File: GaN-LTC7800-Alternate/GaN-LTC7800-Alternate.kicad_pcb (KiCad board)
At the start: 2 copper layers, 86.2 x 46.5 mm, 40 parts, among them Q1 EPC2014C, Q2 EPC2014C, U1 LTC7800HUDC_PBF

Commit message: Updated for preassembly
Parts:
- added RLOAD2: 2Ohm, Resistor_SMD:R_0201_0603Metric, F.Cu at (121.3, 46.0)
- C1, C2, C3, C5, C6, COUT1, CSENSE1, CinA1, CinA2: footprint Capacitor_SMD:C_0805_2012Metric_Pad1.18x1.45mm_HandSolder -> Capacitor_SMD:C_0805_2012Metric
- CinB1: footprint Capacitor_SMD:C_0805_2012Metric_Pad1.18x1.45mm_HandSolder -> Capacitor_Tantalum_SMD:CP_EIA-7343-31_Kemet-D
- R1, R2, R4, R5, R6, R7, R9, RSENSE1: footprint Resistor_SMD:R_0201_0603Metric_Pad0.64x0.40mm_HandSolder -> Resistor_SMD:R_0201_0603Metric
- RLOAD1: value 5Ohm -> 3Ohm; footprint Resistor_SMD:R_0201_0603Metric_Pad0.64x0.40mm_HandSolder -> Resistor_SMD:R_0201_0603Metric
- moved VSource_GND1 9.13 mm to (120.1, 77.9)
- moved TP_VIN2 9.05 mm to (127.8, 81.0)
- moved CinB1 6.87 mm to (109.9, 79.2), turned to 0 degrees
- moved RLOAD1 6.81 mm to (120.2, 47.0), turned to 45 degrees
- moved R5 1.33 mm to (122.2, 66.9)
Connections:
- RLOAD1 pad 2: GND -> Net-(RLOAD1-Pad2)
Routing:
- net /Vout: track 31.5 -> 35.1 mm
- net /SW: track 68.9 -> 71.9 mm
- net Net-(RLOAD1-Pad2): track 0.00 -> 0.91 mm

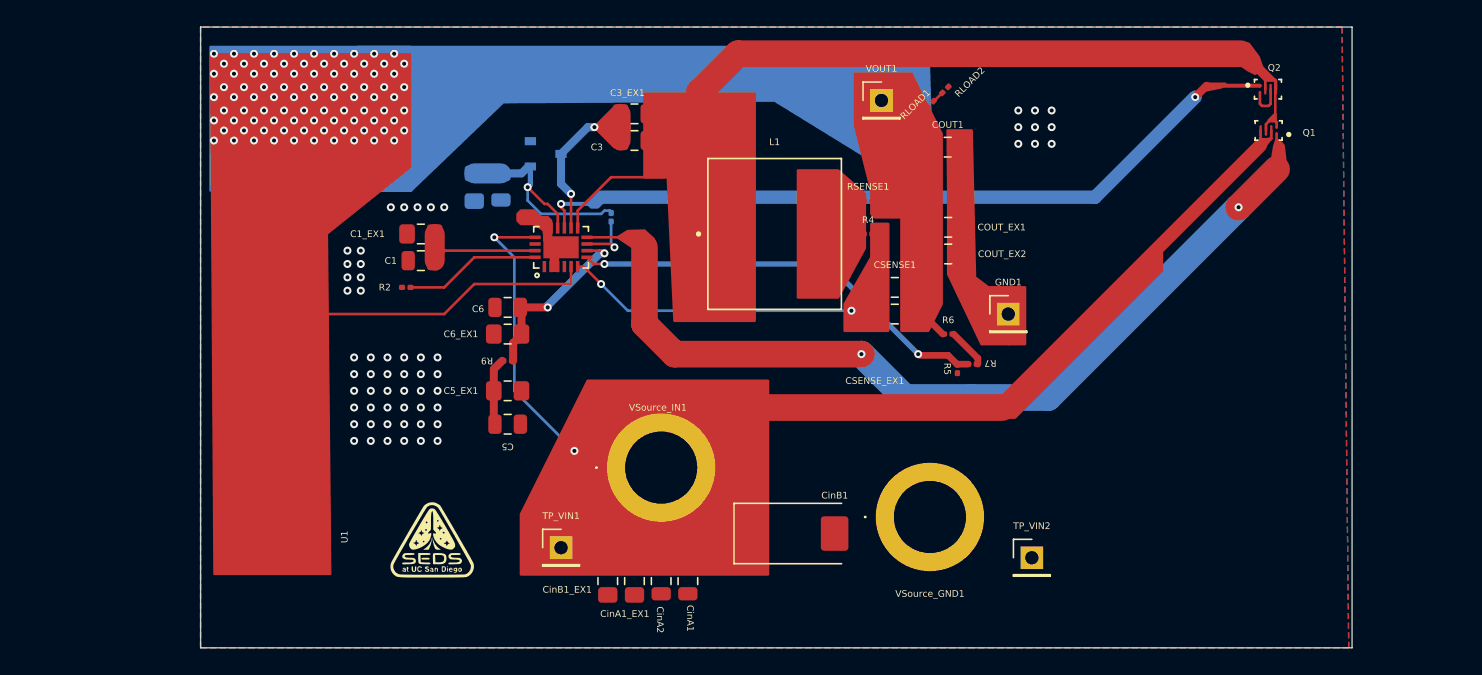
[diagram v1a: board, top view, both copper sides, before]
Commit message: mounting holes
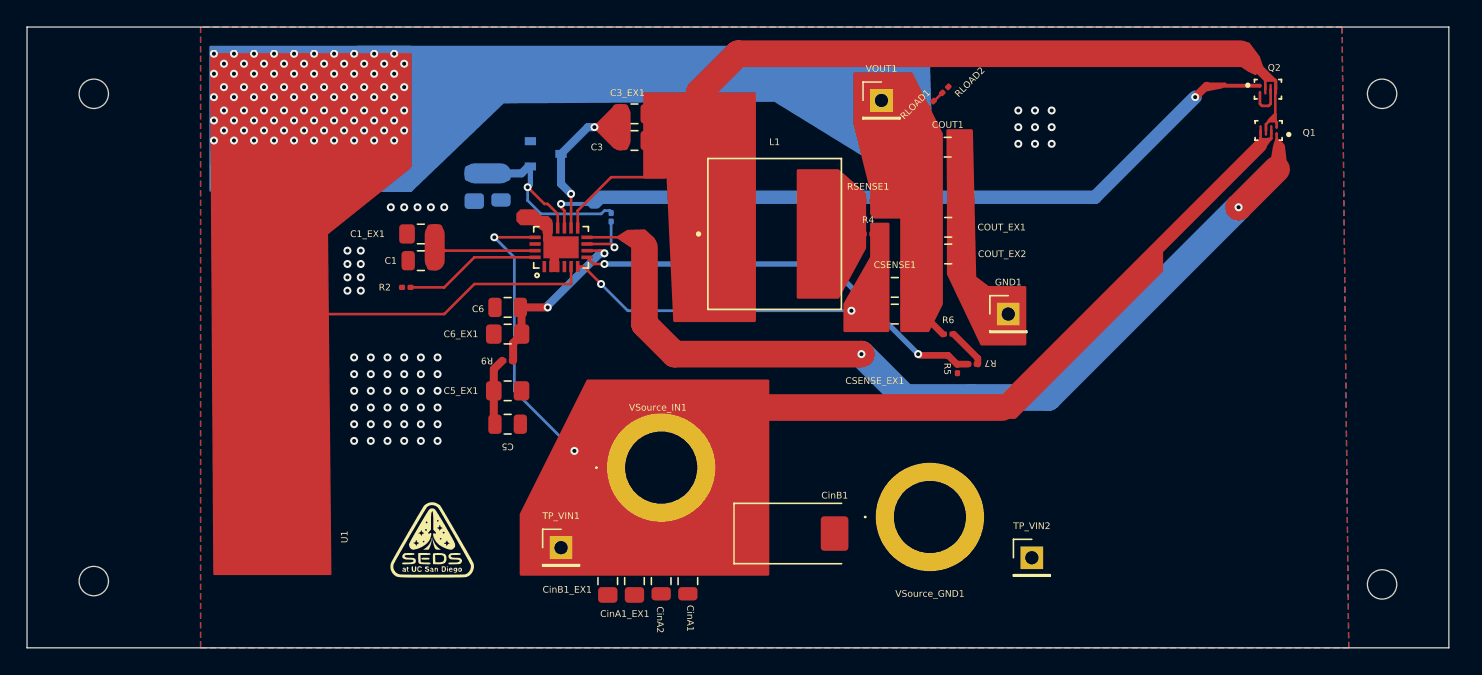
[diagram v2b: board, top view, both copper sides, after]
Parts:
- added REF**: MountingHole_2.2mm_M2, MountingHole:MountingHole_2.2mm_M2, F.Cu at (154.0, 46.2)
- added REF**: MountingHole_2.2mm_M2, MountingHole:MountingHole_2.2mm_M2, F.Cu at (57.5, 82.8)
- added REF**: MountingHole_2.2mm_M2, MountingHole:MountingHole_2.2mm_M2, F.Cu at (57.5, 46.2)
- added REF**: MountingHole_2.2mm_M2, MountingHole:MountingHole_2.2mm_M2, F.Cu at (154.0, 83.0)
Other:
- board size 86.2 x 46.5 mm -> 106.5 x 46.5 mm

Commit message: minor edits
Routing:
- net /INTVCC: track 18.0 -> 14.0 mm
- net Net-(U1-PGOOD): track 4.10 -> 3.30 mm
- net /ITH: track 13.6 -> 12.9 mm
